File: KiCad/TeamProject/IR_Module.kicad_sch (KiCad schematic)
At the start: 21 parts, among them U1 MCP6294, U2 LM339AN, U3 LM339AN

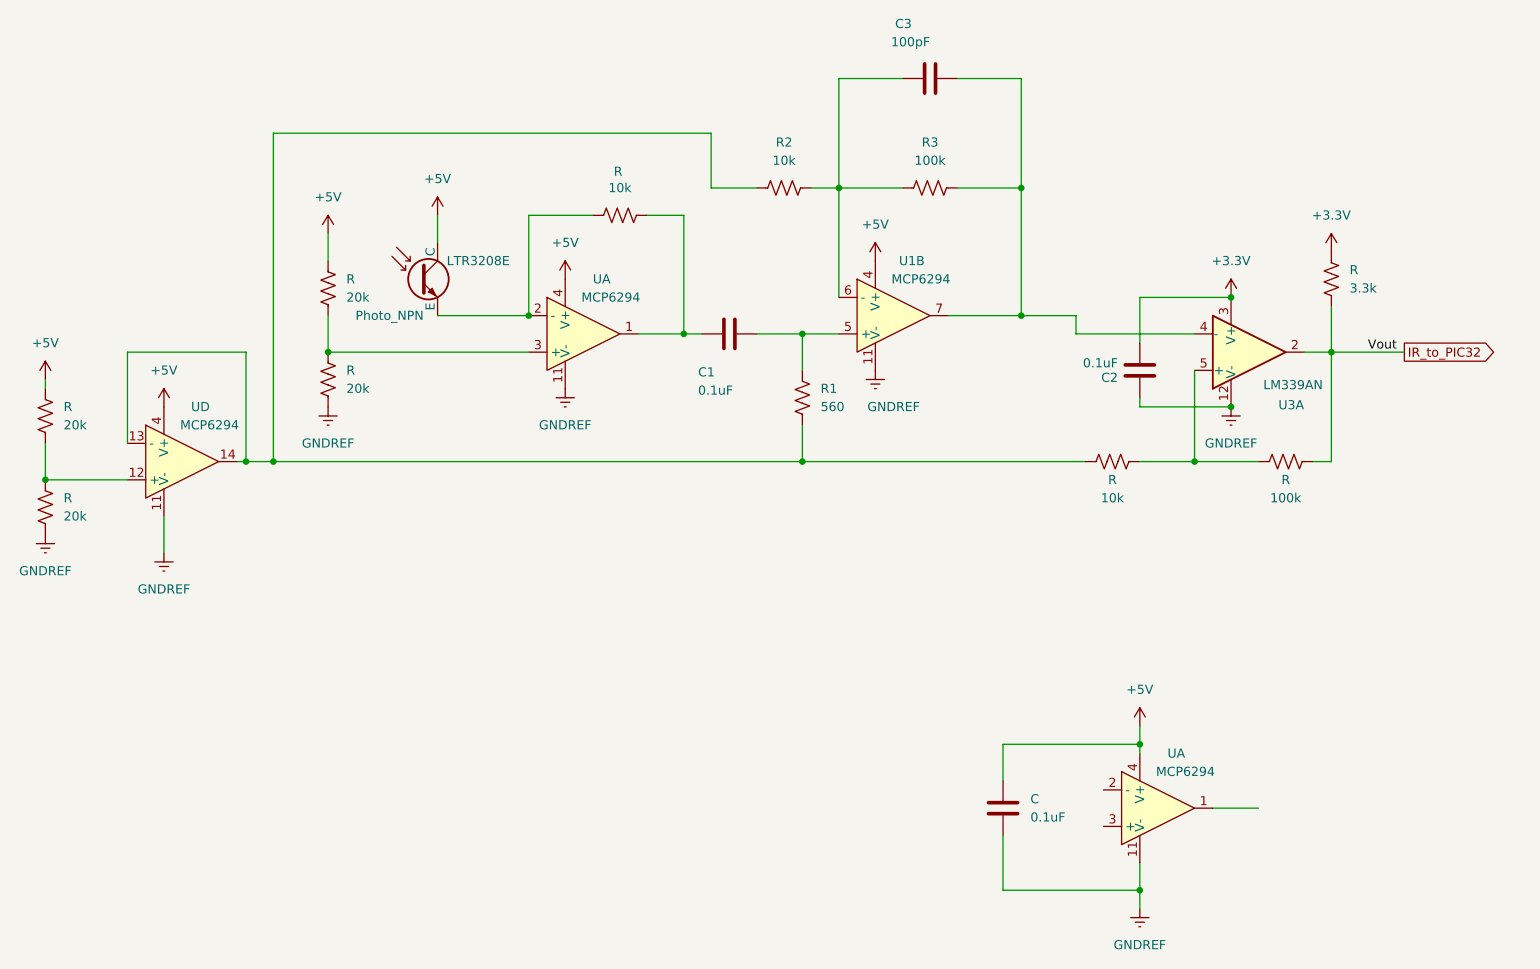
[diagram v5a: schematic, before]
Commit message: Update IR detection schematics
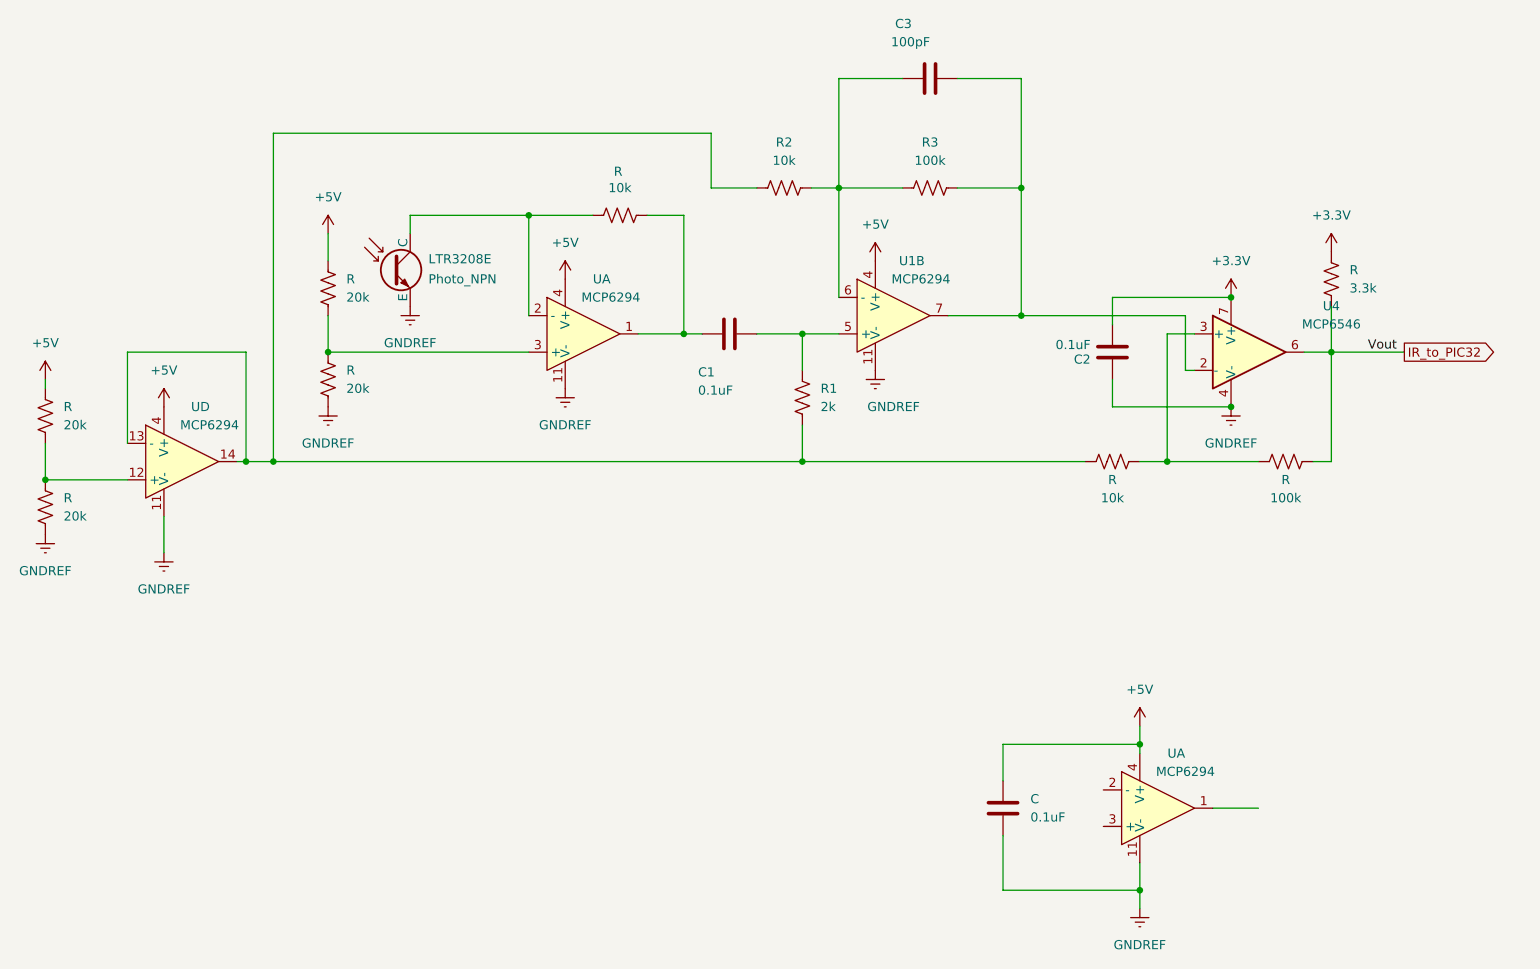
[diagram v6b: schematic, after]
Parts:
- removed U2, U3: LM339AN, symbol ME218_BaseLib:LM339AN
- added U4: MCP6546, symbol ME218_BaseLib:MCP6546
- R1: value 560 -> 2k
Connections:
- net +3.3V: now also U4.7 (V+)
- net +5V: no longer LTR3208E.1 (C)
- net GNDREF: now also LTR3208E.2 (E), U4.4 (V-)
- net IR_to_PIC32: now also U4.6
- net at C3.1, R3.2, U1.7: now also U4.2 (-)
- net at R.1, R.2: now also U4.3 (+)
- net at R.1, U.2 (-): now also LTR3208E.1 (C); no longer LTR3208E.2 (E)
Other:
- moved on the sheet: C2, LTR3208E

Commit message: Replace shooting stepper with servo, add ball lifting servo with no pin available on follower, add side indicator servo to leader
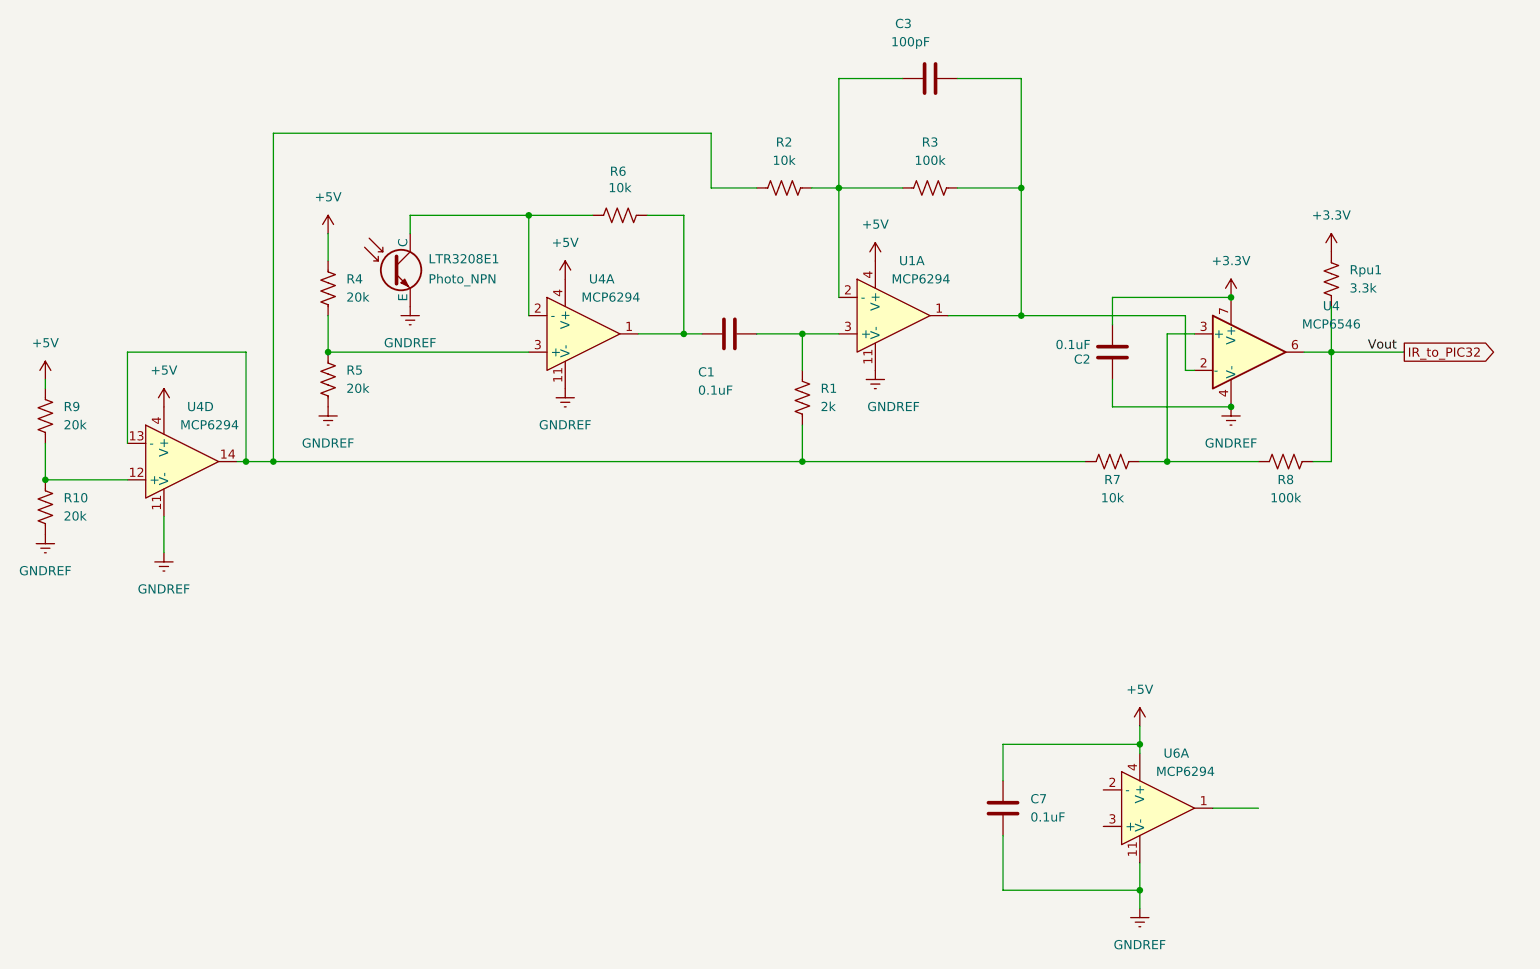
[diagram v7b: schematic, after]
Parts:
- renumbered C to C7, LTR3208E to LTR3208E1, R to R10, R to R4, R to R5, R to R6, R to R7, R to R8, R to R9, R to Rpu1, U to U4, U to U6
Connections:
- net at C1.1, R1.2: now also U1.3 (+); no longer U1.5 (+)
- net at C3.2, R2.2, R3.1: now also U1.2 (-); no longer U1.6 (-)
- net at C3.1, R3.2, U4.2 (-): now also U1.1; no longer U1.7
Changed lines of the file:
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@@
 		(on_board yes)
 		(dnp no)
-		(property "Reference" "#PWR02"
+		(property "Reference" "#PWR?"
 			(at 166.37 90.17 0)
 			(effects
@@
 				)
 			)
+			(project "Leader"
+				(path "/e69a436c-b634-4c28-b262-47742fc47b6f/415f1343-5bea-4de7-9b3a-ad5b76fd5938"
+					(reference "#PWR?")
+					(unit 1)
+				)
+			)
 		)
 	)
@@
 		(on_board yes)
 		(dnp no)
-		(property "Reference" "C2"
+		(property "Reference" "C?"
 			(at 196.342 82.296 0)
 			(effects
@@
 				)
 			)
+			(project "Leader"
+				(path "/e69a436c-b634-4c28-b262-47742fc47b6f/415f1343-5bea-4de7-9b3a-ad5b76fd5938"
+					(reference "C?")
+					(unit 1)
+				)
+			)
 		)
 	)
@@
 		(lib_id "ME218_BaseLib:MCP6294")
 		(at 168.91 76.2 0)
-		(unit 2)
-		(exclude_from_sim no)
-		(in_bom yes)
-		(on_board yes)
-		(dnp no)
-		(property "Reference" "U1"
+		(unit 1)
+		(exclude_from_sim no)
+		(in_bom yes)
+		(on_board yes)
+		(dnp no)
+		(property "Reference" "U?"
 			(at 171.45 68.58 0)
 			(effects
@@
 				)
 			)
+			(project "Leader"
+				(path "/e69a436c-b634-4c28-b262-47742fc47b6f/415f1343-5bea-4de7-9b3a-ad5b76fd5938"
+					(reference "U?")
+					(unit 1)
+				)
+			)
 		)
 	)
@@
 		(on_board yes)
 		(dnp no)
-		(property "Reference" "R"
+		(property "Reference" "R7"
 			(at 199.39 99.06 90)
 			(effects
@@
 		(dnp no)
 		(fields_autoplaced yes)
-		(property "Reference" "R3"
+		(property "Reference" "R?"
 			(at 173.99 52.07 90)
 			(effects
@@
 				)
 			)
+			(project "Leader"
+				(path "/e69a436c-b634-4c28-b262-47742fc47b6f/415f1343-5bea-4de7-9b3a-ad5b76fd5938"
+					(reference "R?")
+					(unit 1)
+				)
+			)
 		)
 	)
@@
 		(dnp no)
 		(fields_autoplaced yes)
-		(property "Reference" "R1"
+		(property "Reference" "R?"
 			(at 158.75 86.3599 0)
 			(effects
@@
 				)
 			)
+			(project "Leader"
+				(path "/e69a436c-b634-4c28-b262-47742fc47b6f/415f1343-5bea-4de7-9b3a-ad5b76fd5938"
+					(reference "R?")
+					(unit 1)
+				)
+			)
 		)
 	)
@@
 		(dnp no)
 		(fields_autoplaced yes)
-		(property "Reference" "#PWR03"
+		(property "Reference" "#PWR?"
 			(at 101.6 81.28 0)
 			(effects
@@
 				)
 			)
+			(project "Leader"
+				(path "/e69a436c-b634-4c28-b262-47742fc47b6f/415f1343-5bea-4de7-9b3a-ad5b76fd5938"
+					(reference "#PWR?")
+					(unit 1)
+				)
+			)
 		)
 	)
@@
 		(dnp no)
 		(fields_autoplaced yes)
-		(property "Reference" "#PWR?"
+		(property "Reference" "#PWR09"
 			(at 90.17 95.25 0)
 			(effects
@@
 		(on_board yes)
 		(dnp no)
-		(property "Reference" "R"
+		(property "Reference" "R8"
 			(at 223.52 99.06 90)
 			(effects
@@
 		(dnp no)
 		(fields_autoplaced yes)
-		(property "Reference" "R"
+		(property "Reference" "R9"
 			(at 53.34 88.8999 0)
 			(effects
@@
 		(dnp no)
 		(fields_autoplaced yes)
-		(property "Reference" "#PWR01"
+		(property "Reference" "#PWR?"
 			(at 166.37 72.39 0)
 			(effects
@@
 				)
 			)
+			(project "Leader"
+				(path "/e69a436c-b634-4c28-b262-47742fc47b6f/415f1343-5bea-4de7-9b3a-ad5b76fd5938"
+					(reference "#PWR?")
+					(unit 1)
+				)
+			)
 		)
 	)
@@
 		(on_board yes)
 		(dnp no)
-		(property "Reference" "U4"
+		(property "Reference" "U?"
 			(at 229.87 74.8598 0)
 			(effects
@@
 				)
 			)
+			(project "Leader"
+				(path "/e69a436c-b634-4c28-b262-47742fc47b6f/415f1343-5bea-4de7-9b3a-ad5b76fd5938"
+					(reference "U?")
+					(unit 1)
+				)
+			)
 		)
 	)
@@
 		(dnp no)
 		(fields_autoplaced yes)
-		(property "Reference" "#PWR?"
+		(property "Reference" "#PWR029"
 			(at 215.9 77.47 0)
 			(effects
@@
 		(dnp no)
 		(fields_autoplaced yes)
-		(property "Reference" "#PWR?"
+		(property "Reference" "#PWR032"
 			(at 67.31 115.57 0)
 			(effects
@@
 		(on_board yes)
 		(dnp no)
-		(property "Reference" "C1"
+		(property "Reference" "C?"
 			(at 144.018 84.074 90)
 			(effects
@@
 				)
 			)
+			(project "Leader"
+				(path "/e69a436c-b634-4c28-b262-47742fc47b6f/415f1343-5bea-4de7-9b3a-ad5b76fd5938"
+					(reference "C?")
+					(unit 1)
+				)
+			)
 		)
 	)
@@
 		(dnp no)
 		(fields_autoplaced yes)
-		(property "Reference" "#PWR?"
+		(property "Reference" "#PWR023"
 			(at 123.19 74.93 0)
 			(effects
@@
 		(on_board yes)
 		(dnp no)
-		(property "Reference" "C3"
+		(property "Reference" "C?"
 			(at 171.45 35.56 90)
 			(effects
@@
 				)
 			)
+			(project "Leader"
+				(path "/e69a436c-b634-4c28-b262-47742fc47b6f/415f1343-5bea-4de7-9b3a-ad5b76fd5938"
+					(reference "C?")
+					(unit 1)
+				)
+			)
 		)
 	)
@@
 		(dnp no)
 		(fields_autoplaced yes)
-		(property "Reference" "C"
+		(property "Reference" "C7"
 			(at 187.96 143.5099 0)
 			(effects
@@
 		(dnp no)
 		(fields_autoplaced yes)
-		(property "Reference" "#PWR?"
+		(property "Reference" "#PWR030"
 			(at 215.9 95.25 0)
 			(effects
@@
 		(dnp no)
 		(fields_autoplaced yes)
-		(property "Reference" "#PWR?"
+		(property "Reference" "#PWR024"
 			(at 123.19 92.71 0)
 			(effects
@@
 		(dnp no)
 		(fields_autoplaced yes)
-		(property "Reference" "#PWR?"
+		(property "Reference" "#PWR021"
 			(at 50.8 113.03 0)
 			(effects
@@
 		(dnp no)
 		(fields_autoplaced yes)
-		(property "Reference" "#PWR?"
+		(property "Reference" "#PWR031"
 			(at 67.31 92.71 0)
 			(effects
@@
 		(on_board yes)
 		(dnp no)
-		(property "Reference" "U"
+		(property "Reference" "U4"
 			(at 72.39 88.9 0)
 			(effects
@@
 		(dnp no)
 		(fields_autoplaced yes)
-		(property "Reference" "#PWR?"
+		(property "Reference" "#PWR020"
 			(at 50.8 88.9 0)
 			(effects
@@
 		(dnp no)
 		(fields_autoplaced yes)
-		(property "Reference" "R"
+		(property "Reference" "Rpu1"
 			(at 232.41 69.8499 0)
 			(effects
@@
 		(on_board yes)
 		(dnp no)
-		(property "Reference" "LTR3208E"
+		(property "Reference" "LTR3208E1"
 			(at 104.14 68.326 0)
 			(effects
@@
 		(dnp no)
 		(fields_autoplaced yes)
-		(property "Reference" "R"
+		(property "Reference" "R10"
 			(at 53.34 101.5999 0)
 			(effects
@@
 		(on_board yes)
 		(dnp no)
-		(property "Reference" "R"
+		(property "Reference" "R6"
 			(at 130.556 56.134 90)
 			(effects
@@
 		(on_board yes)
 		(dnp no)
-		(property "Reference" "U"
+		(property "Reference" "U4"
 			(at 128.27 71.12 0)
 			(effects
@@
 		(dnp no)
 		(fields_autoplaced yes)
-		(property "Reference" "R"
+		(property "Reference" "R5"
 			(at 92.71 83.8199 0)
 			(effects
@@
 		(dnp no)
 		(fields_autoplaced yes)
-		(property "Reference" "#PWR?"
+		(property "Reference" "#PWR027"
 			(at 229.87 71.12 0)
 			(effects
@@
 		(dnp no)
 		(fields_autoplaced yes)
-		(property "Reference" "#PWR?"
+		(property "Reference" "#PWR025"
 			(at 203.2 137.16 0)
 			(effects
@@
 		(dnp no)
 		(fields_autoplaced yes)
-		(property "Reference" "#PWR?"
+		(property "Reference" "#PWR026"
 			(at 203.2 165.1 0)
 			(effects
@@
 		(on_board yes)
 		(dnp no)
-		(property "Reference" "U"
+		(property "Reference" "U6"
 			(at 208.28 137.16 0)
 			(effects
@@
 		(dnp no)
 		(fields_autoplaced yes)
-		(property "Reference" "#PWR?"
+		(property "Reference" "#PWR08"
 			(at 90.17 68.58 0)
 			(effects
@@
 		(dnp no)
 		(fields_autoplaced yes)
-		(property "Reference" "R"
+		(property "Reference" "R4"
 			(at 92.71 71.1199 0)
 			(effects
@@
 		(dnp no)
 		(fields_autoplaced yes)
-		(property "Reference" "R2"
+		(property "Reference" "R?"
 			(at 153.67 52.07 90)
 			(effects
@@
 					(unit 1)
 				)
+			)
+			(project "Leader"
+				(path "/e69a436c-b634-4c28-b262-47742fc47b6f/415f1343-5bea-4de7-9b3a-ad5b76fd5938"
+					(reference "R?")
+					(unit 1)
+				)

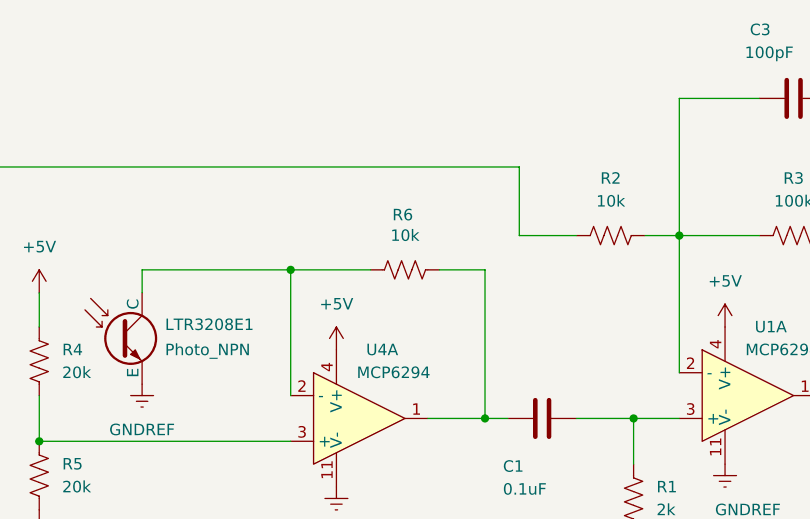
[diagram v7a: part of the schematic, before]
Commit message: Refactoring DCMotorService on LeaderPIC in progress
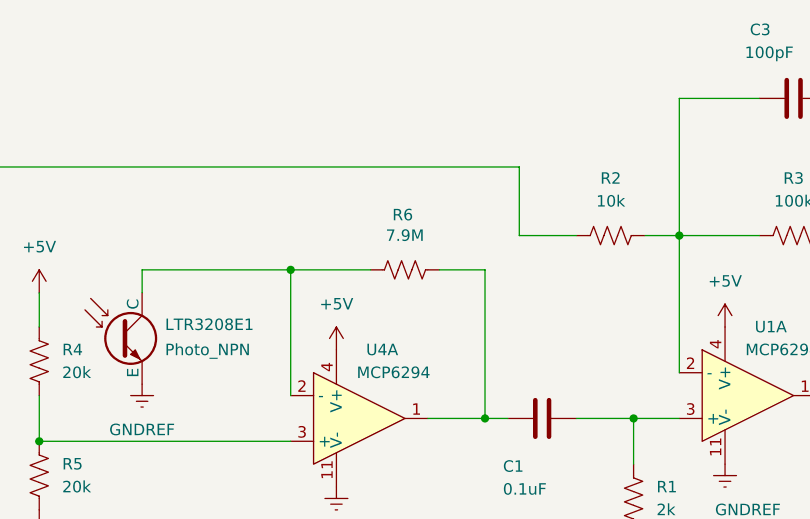
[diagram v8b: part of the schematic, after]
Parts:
- R6: value 10k -> 7.9M
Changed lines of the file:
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@@
 			)
 		)
-		(property "Value" "10k"
+		(property "Value" "7.9M"
 			(at 130.81 58.42 90)
 			(effects
